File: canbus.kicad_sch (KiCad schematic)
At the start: 7 parts, among them J201 Conn_01x05, U201 SN65HVD232DR

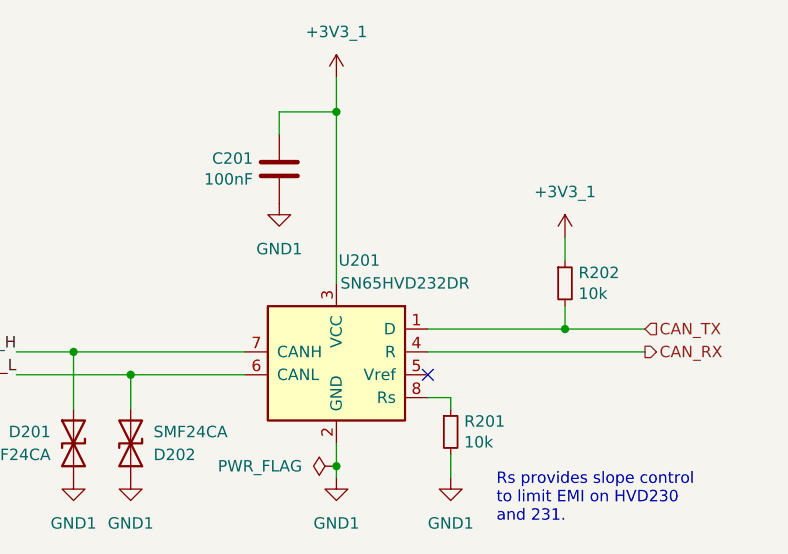
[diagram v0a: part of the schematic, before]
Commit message: Change CAN transceiver according to availability
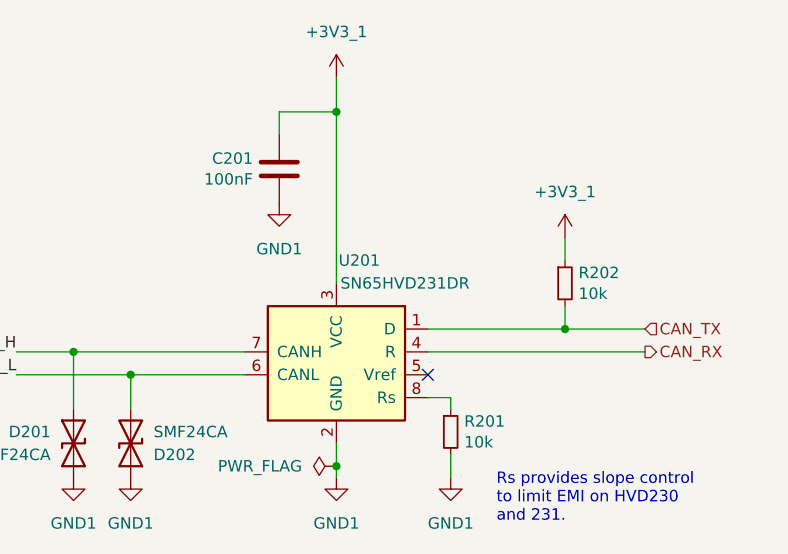
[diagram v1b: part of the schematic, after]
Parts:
- U201: value SN65HVD232DR -> SN65HVD231DR; LCSC C30530 -> C129257
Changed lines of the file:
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@@
     (in_bom yes) (on_board yes)
     (property "Reference" "U201" (id 0) (at 137.16 100.33 0))
-    (property "Value" "SN65HVD232DR" (id 1) (at 142.24 102.87 0))
+    (property "Value" "SN65HVD231DR" (id 1) (at 142.24 102.87 0))
     (property "Footprint" "Package_SO:SOIC-8_3.9x4.9mm_P1.27mm" (id 2) (at 134.62 123.19 0)
       (effects (font (size 1.27 1.27)) hide)
@@
       (effects (font (size 1.27 1.27)) hide)
     )
-    (property "LCSC" "C30530" (id 4) (at 134.62 110.49 0)
+    (property "LCSC" "C129257" (id 4) (at 134.62 110.49 0)
       (effects (font (size 1.27 1.27)) hide)
     )

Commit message: Update TVS diode LCSC part number
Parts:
- D201, D202: LCSC C466521 -> C353294
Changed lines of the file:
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@@
       (effects (font (size 1.27 1.27)) hide)
     )
-    (property "LCSC" "C466521" (id 4) (at 111.76 120.65 90)
+    (property "LCSC" "C353294" (id 4) (at 111.76 120.65 90)
       (effects (font (size 1.27 1.27)) hide)
     )
@@
       (effects (font (size 1.27 1.27)) hide)
     )
-    (property "LCSC" "C466521" (id 4) (at 105.41 120.65 90)
+    (property "LCSC" "C353294" (id 4) (at 105.41 120.65 90)
       (effects (font (size 1.27 1.27)) hide)
     )
